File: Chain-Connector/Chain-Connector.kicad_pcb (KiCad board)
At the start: 2 copper layers, 24.1 x 21.6 mm, 11 parts, among them P1 USB_A, P2 CONN_01X06, U1 SN74HC157PWR

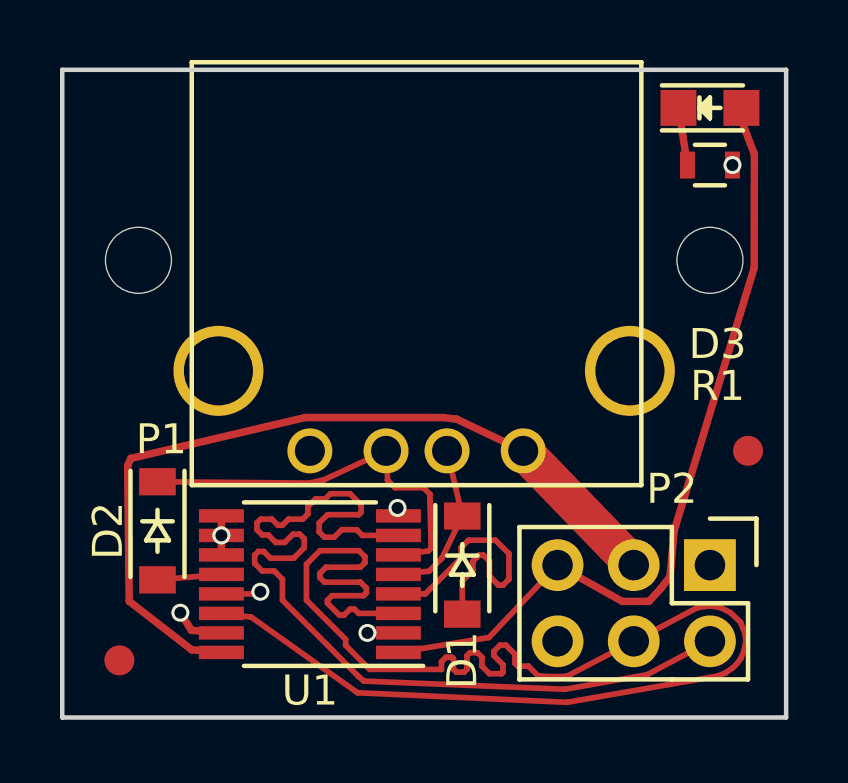
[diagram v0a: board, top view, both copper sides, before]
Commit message: Switched to 2.5mm Mounting Holes
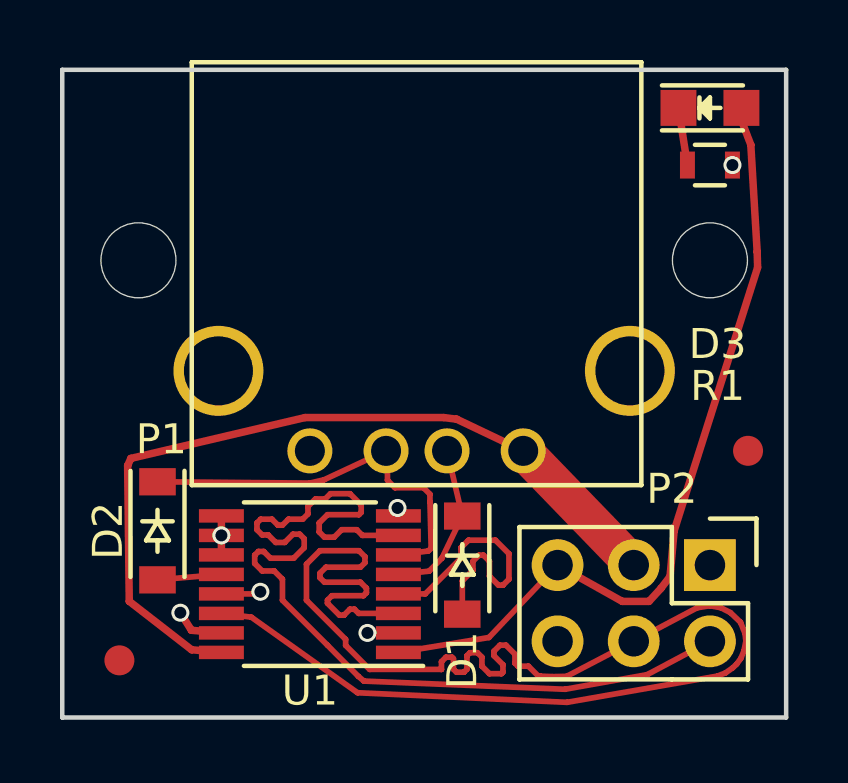
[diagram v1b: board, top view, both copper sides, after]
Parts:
- removed the ? at (139.7, 90.2)
- removed the ? at (158.8, 90.2)
- added ?: MountingHole_2.5mm, Mounting_Holes:MountingHole_2.5mm, F.Cu at (139.7, 90.2)
- added ?: MountingHole_2.5mm, Mounting_Holes:MountingHole_2.5mm, F.Cu at (158.8, 90.2)
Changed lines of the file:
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@@
     (thickness 1.6)
     (drawings 4)
-    (tracks 202)
+    (tracks 203)
     (zones 0)
     (modules 11)
@@
     (add_net VCC)
   )
+  (module Mounting_Holes:MountingHole_2.5mm (layer F.Cu)
+    (at 139.7 90.17)
+    (descr "Mounting Hole 2.5mm, no annular")
+    (tags "mounting hole 2.5mm no annular")
+    (fp_text reference "" (at 0 0) (layer F.SilkS) hide
+      (effects (font (size 0.127 0.127) (thickness 0.000001)))
+    )
+    (fp_text value MountingHole_2.5mm (at 0 3.5) (layer F.Fab)
+      (effects (font (size 1 1) (thickness 0.15)))
+    )
+    (fp_circle (center 0 0) (end 2.5 0) (layer Cmts.User) (width 0.15))
+    (fp_circle (center 0 0) (end 2.75 0) (layer F.CrtYd) (width 0.05))
+    (pad 1 np_thru_hole circle (at 0 0) (size 2.5 2.5) (drill 2.5) (layers *.Cu *.Mask F.SilkS))
+  )
+  (module Mounting_Holes:MountingHole_2.5mm (layer F.Cu)
+    (at 158.75 90.17)
+    (descr "Mounting Hole 2.5mm, no annular")
+    (tags "mounting hole 2.5mm no annular")
+    (fp_text reference "" (at 0 0) (layer F.SilkS) hide
+      (effects (font (size 0.127 0.127) (thickness 0.000001)))
+    )
+    (fp_text value MountingHole_2.5mm (at 0 3.5) (layer F.Fab)
+      (effects (font (size 1 1) (thickness 0.15)))
+    )
+    (fp_circle (center 0 0) (end 2.5 0) (layer Cmts.User) (width 0.15))
+    (fp_circle (center 0 0) (end 2.75 0) (layer F.CrtYd) (width 0.05))
+    (pad 1 np_thru_hole circle (at 0 0) (size 2.5 2.5) (drill 2.5) (layers *.Cu *.Mask F.SilkS))
+  )
   (module Fiducials:Fiducial_1mm_Dia_2.54mm_Outer_CopperTop (layer F.Cu)
     (at 160.02 96.52)
@@
     (pad ~ smd circle (at 0 0) (size 1 1) (layers F.Cu F.Mask)
       (solder_mask_margin 0.77) (clearance 0.77))
-  )
-  (module Mounting_Holes:MountingHole_2.2mm_M2_ISO14580 (layer F.Cu)
-    (at 139.7 90.17)
-    (descr "Mounting Hole 2.2mm, no annular, M2, ISO14580")
-    (tags "mounting hole 2.2mm no annular m2 iso14580")
-    (fp_text reference "" (at 0 0) (layer F.SilkS) hide
-      (effects (font (size 0.127 0.127) (thickness 0.000001)))
-    )
-    (fp_text value MountingHole_2.2mm_M2_ISO14580 (at 0 2.9) (layer F.Fab)
-      (effects (font (size 1 1) (thickness 0.15)))
-    )
-    (fp_circle (center 0 0) (end 1.9 0) (layer Cmts.User) (width 0.15))
-    (fp_circle (center 0 0) (end 2.15 0) (layer F.CrtYd) (width 0.05))
-    (pad 1 np_thru_hole circle (at 0 0) (size 2.2 2.2) (drill 2.2) (layers *.Cu *.Mask F.SilkS))
   )
   (module Connect:USB_A (layer F.Cu)
@@
       (rotate (xyz 0 0 90))
     )
-  )
-  (module Mounting_Holes:MountingHole_2.2mm_M2_ISO14580 (layer F.Cu)
-    (at 158.75 90.17)
-    (descr "Mounting Hole 2.2mm, no annular, M2, ISO14580")
-    (tags "mounting hole 2.2mm no annular m2 iso14580")
-    (fp_text reference "" (at 0 0) (layer F.SilkS) hide
-      (effects (font (size 0.127 0.127) (thickness 0.000001)))
-    )
-    (fp_text value MountingHole_2.2mm_M2_ISO14580 (at 0 2.9) (layer F.Fab)
-      (effects (font (size 1 1) (thickness 0.15)))
-    )
-    (fp_circle (center 0 0) (end 1.9 0) (layer Cmts.User) (width 0.15))
-    (fp_circle (center 0 0) (end 2.15 0) (layer F.CrtYd) (width 0.05))
-    (pad 1 np_thru_hole circle (at 0 0) (size 2.2 2.2) (drill 2.2) (layers *.Cu *.Mask F.SilkS))
   )
   (module Diodes_SMD:SOD-123 (layer F.Cu)
@@
   (segment (start 157.115672 101.107326) (end 156.718005 101.539919) (width 0.25) (layer F.Cu) (net 7))
   (segment (start 159.79902 85.09) (end 159.79902 85.50402) (width 0.25) (layer F.Cu) (net 7) (status 30))
-  (segment (start 159.79902 85.50402) (end 160.2315 86.630319) (width 0.25) (layer F.Cu) (net 7) (status 10))
-  (segment (start 160.2315 86.630319) (end 160.224138 90.423903) (width 0.25) (layer F.Cu) (net 7))
-  (segment (start 160.224138 90.423903) (end 157.55717 99.182514) (width 0.25) (layer F.Cu) (net 7))
+  (segment (start 159.79902 85.50402) (end 160.111888 86.318823) (width 0.25) (layer F.Cu) (net 7) (status 10))
+  (segment (start 160.111888 86.318823) (end 160.323862 89.888842) (width 0.25) (layer F.Cu) (net 7))
+  (segment (start 160.323862 89.888842) (end 160.338619 90.409468) (width 0.25) (layer F.Cu) (net 7))
+  (segment (start 160.338619 90.409468) (end 157.55717 99.182514) (width 0.25) (layer F.Cu) (net 7))
   (segment (start 157.70098 85.09) (end 158 86.995) (width 0.25) (layer F.Cu) (net 8) (status 30))
   (segment (start 141.097 101.9175) (end 141.4653 102.5017) (width 0.25) (layer F.Cu) (net 9))
